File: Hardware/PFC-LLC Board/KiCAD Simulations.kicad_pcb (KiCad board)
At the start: 2 copper layers, 217.4 x 136.9 mm, 111 parts, among them J1 1792229, J2 Conn_01x02_Female, J3 1792229, J4 1792229, J5 Conn_01x02_Female, J6 1792229, Q1 C2M0160120D, U1 UCC28180DR, U1LLC1 UCC256403DDBR, U2LLC1 UCC24624DT

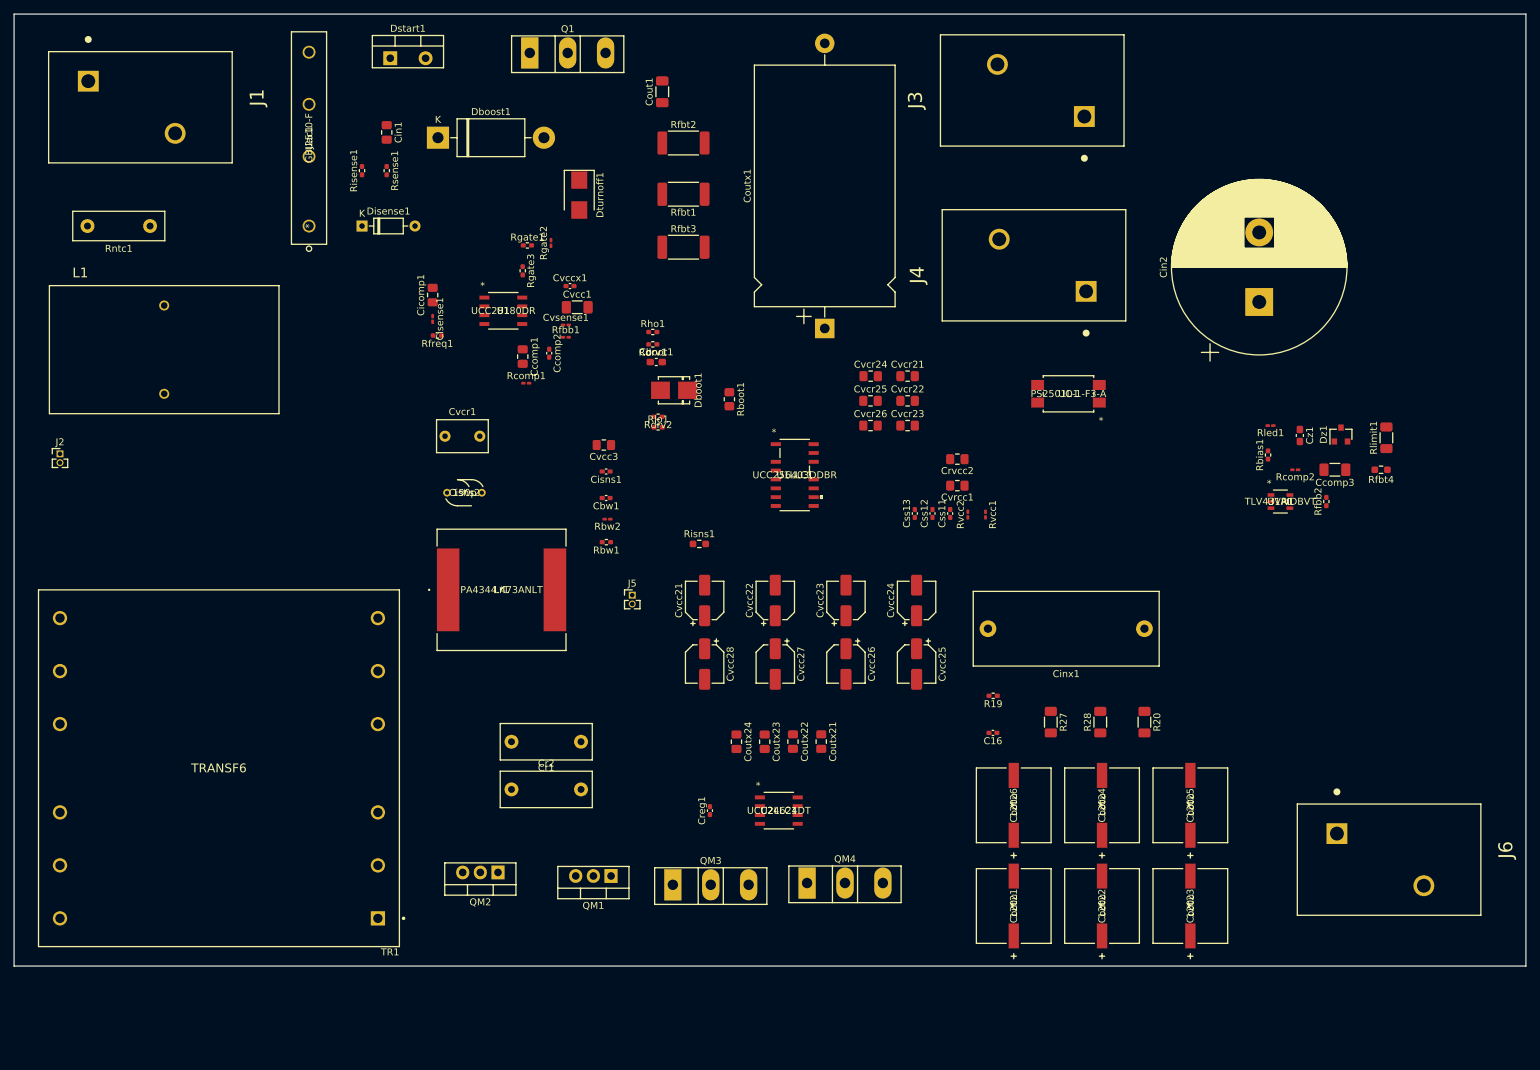
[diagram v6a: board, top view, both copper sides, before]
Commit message: layout done with some routing for LLC
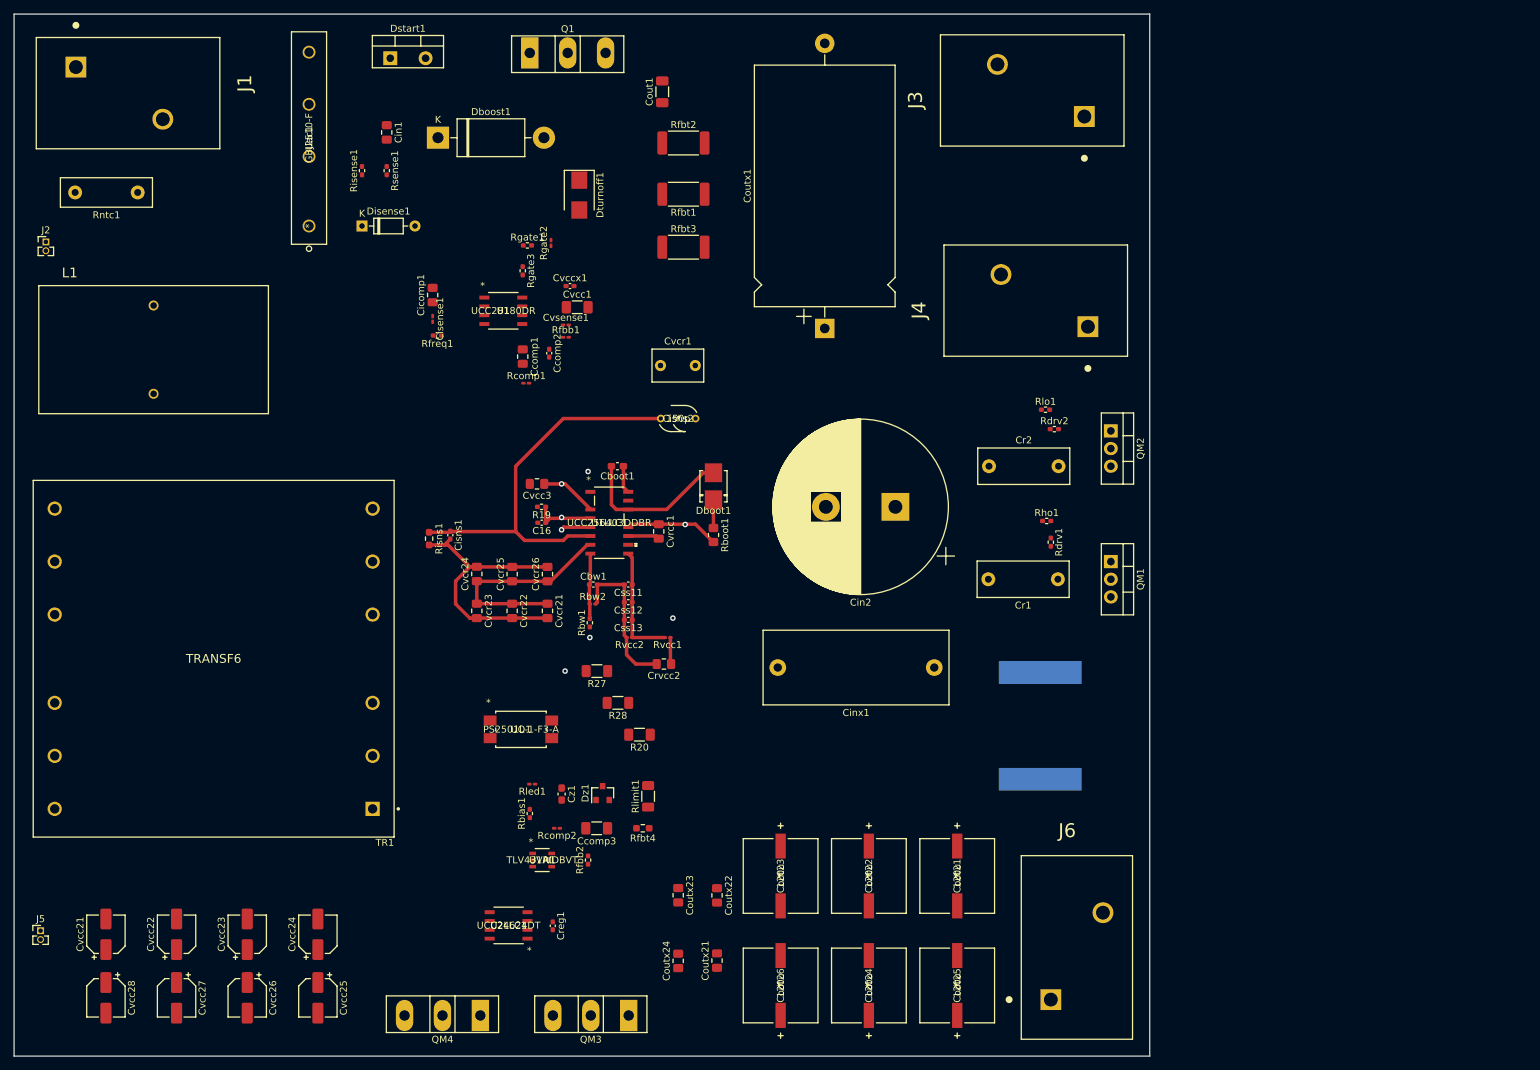
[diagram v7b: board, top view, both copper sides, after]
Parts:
- Lr1: moved to B.Cu
- moved UVR1 118.0 mm to (126.7, 137.2)
- moved Ccomp3 118.0 mm to (134.6, 132.6)
- moved Cz1 118.0 mm to (129.5, 127.7)
- moved Dz1 118.0 mm to (135.4, 127.5)
- moved Rcomp2 118.0 mm to (128.9, 132.6)
- moved Rfbb2 118.0 mm to (133.3, 137.2)
- moved Rfbt4 118.0 mm to (141.2, 132.6)
- moved Rlimit1 118.0 mm to (142.0, 128.0)
- moved Rbias1 118.0 mm to (125.0, 130.5)
- moved Rled1 118.0 mm to (125.3, 126.2)
- moved QM2 108.6 mm to (208.5, 75.4), turned to 270 degrees
- moved Cvcc21 98.6 mm to (64.0, 147.8)
- moved Cvcc28 98.6 mm to (64.0, 157.0)
- moved Cvcc22 98.6 mm to (74.2, 147.8)
- moved Cvcc23 98.6 mm to (84.3, 147.8)
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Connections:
- J4 pad 1: Net-(Cin2-Pad1) -> GND
- J4 pad 2: GND -> Net-(Cin2-Pad1)
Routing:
- net GND: track 0.08 -> 66.3 mm
- net Net-(Cisns1-Pad1): track 0.00 -> 57.2 mm
- net Net-(Cvcr1-Pad2): track 0.14 -> 31.9 mm
- net Net-(Cboot1-Pad2): track 0.00 -> 22.7 mm
- net Net-(Crvcc2-Pad1): track 0.00 -> 17.3 mm, vias 0 -> 1
- net Net-(Css11-Pad1): track 0.00 -> 17.0 mm
- net Net-(Cbw1-Pad1): track 0.04 -> 9.43 mm
- net /LLC/BLK: track 0.00 -> 8.97 mm, vias 0 -> 1
- net Net-(Cvcc21-Pad1): track 0.48 -> 8.19 mm, vias 0 -> 1
- net Net-(U1LLC1-Pad5): track 0.00 -> 4.26 mm, vias 0 -> 1
- net Net-(Dboot1-Pad1): track 0.00 -> 4.06 mm
- net /LLC/HS: track 0.00 -> 3.97 mm
- net (no net): vias 0 -> 4
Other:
- board size 217.4 x 136.9 mm -> 163.3 x 149.9 mm

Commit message: More progress on routing PCB
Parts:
- Lr1: moved to F.Cu
- moved Cvcr1 5.14 mm to (148.8, 66.8), turned to 180 degrees
- moved Creg1 1.53 mm to (129.8, 146.5)
- moved Cisns1 1.27 mm to (114.8, 90.4)
- moved Risns1 1.27 mm to (111.8, 90.9)
- moved TR1 1.27 mm to (80.8, 108.2)
- moved Lr1 0.76 mm to (198.4, 118.6)
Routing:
- net GND: track 66.3 -> 228.1 mm
- net Net-(Cin2-Pad1): track 0.00 -> 137.4 mm, vias 0 -> 1
- net /LLC/HS: track 3.97 -> 138.2 mm, vias 0 -> 1
- net Net-(Cisns2-Pad2): track 0.00 -> 105.2 mm, vias 0 -> 3
- net /LLC/LO: track 0.00 -> 81.9 mm, vias 0 -> 2
- net /LLC/HO: track 0.00 -> 71.4 mm, vias 0 -> 2
- net GND1: track 0.00 -> 55.2 mm
- net Net-(Cvcr1-Pad2): track 31.9 -> 84.1 mm
- net Net-(Rbias1-Pad2): track 0.11 -> 31.8 mm
- net /LLC/BLK: track 8.97 -> 33.3 mm, vias 1 -> 2
- net Net-(QM4-Pad2): track 0.00 -> 19.2 mm
- net Net-(QM2-Pad1): track 0.00 -> 18.4 mm, vias 0 -> 2
- net Net-(Rbias1-Pad1): track 0.00 -> 18.2 mm
- net Net-(Ccomp3-Pad1): track 0.00 -> 16.9 mm
- net Net-(Cz1-Pad1): track 0.12 -> 16.6 mm
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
